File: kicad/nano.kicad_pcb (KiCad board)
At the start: 4 copper layers, 85 x 56 mm, 228 parts, among them J1 SD-104031, J2 PMIC_I2C, J3 USB_Micro, J4 USB_OTG, J5 JTAG, J6 TOUCH PANEL, J7 LiPo_THM, P1 EXPANSION, P2 DISPLAY, P3 J0011D01BNL, P4 USB-A-D-RA-30, P5 USB-A-D-RA-30, Q1 2SK3018, U1 IMX6UL_BGA289, U10 MIC2506, U11 MIC2506, U12 MIC2877, U2 DDR3_BGA96, U3 A7101CH, U4 W25M512JV, U5 W25M512JV, U6 PF1550, U7 LAN8720A, U8 USB2514B, U9 CP2102N-QFN20, Y1 32.768 kHz

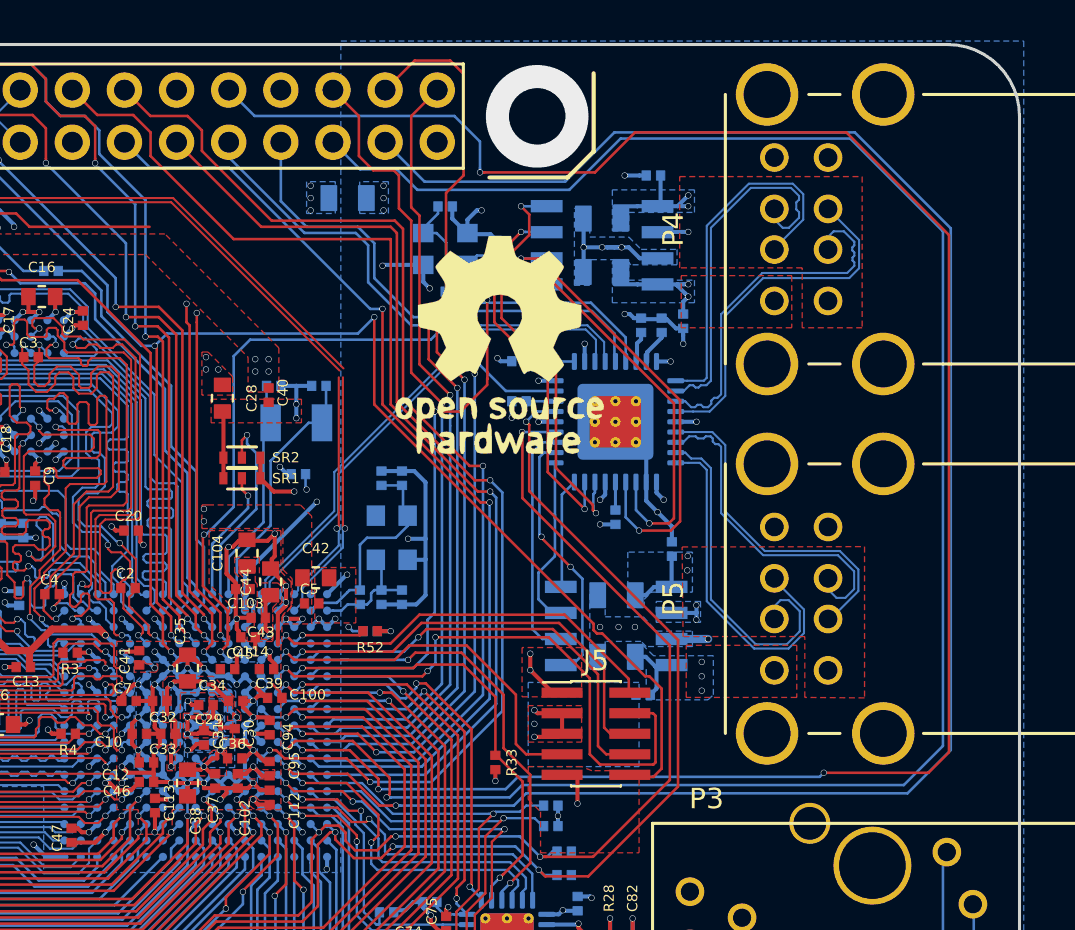
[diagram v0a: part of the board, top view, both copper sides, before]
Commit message: uart2/3 layout
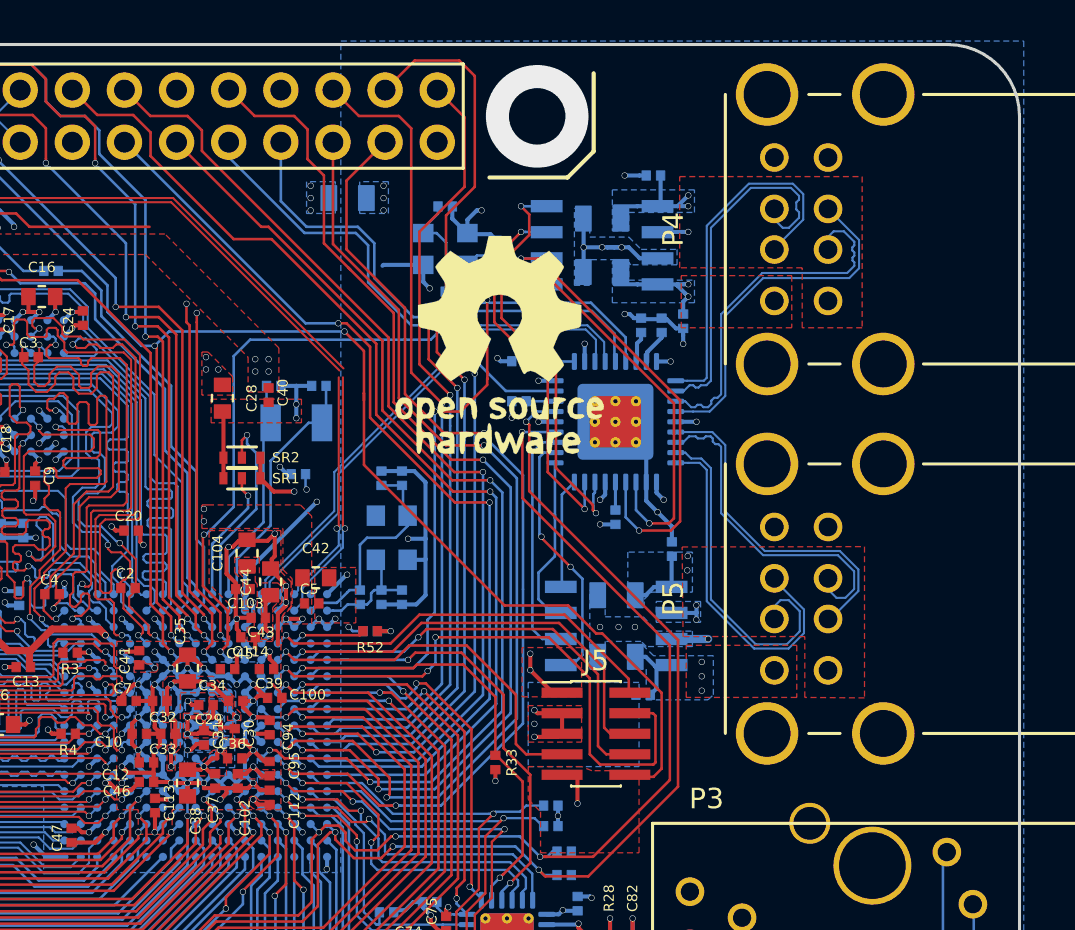
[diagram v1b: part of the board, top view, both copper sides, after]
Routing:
- net /IMX_Peripherals_1/UART3_CTS: track 99.6 -> 51.6 mm, vias 4 -> 3
- net UART2_RTS: track 94.4 -> 48.4 mm, vias 2 -> 3
- net /IMX_Peripherals_1/UART3_RTS: track 91.6 -> 48.4 mm, vias 2 -> 3
- net UART4_TXD: track 50.6 -> 47.5 mm
- net /IMX_Peripherals_1/UART5_RX: track 52.4 -> 49.6 mm
- net /IMX_Peripherals_1/UART5_TX: track 54.0 -> 51.3 mm
- net UART2_RXD: track 38.2 -> 39.0 mm
- net UART2_CTS: track 46.3 -> 47.0 mm
- net UART4_RXD: track 47.6 -> 46.9 mm
- net UART2_TXD: track 38.2 -> 38.7 mm
- net GND: vias 154 -> 153

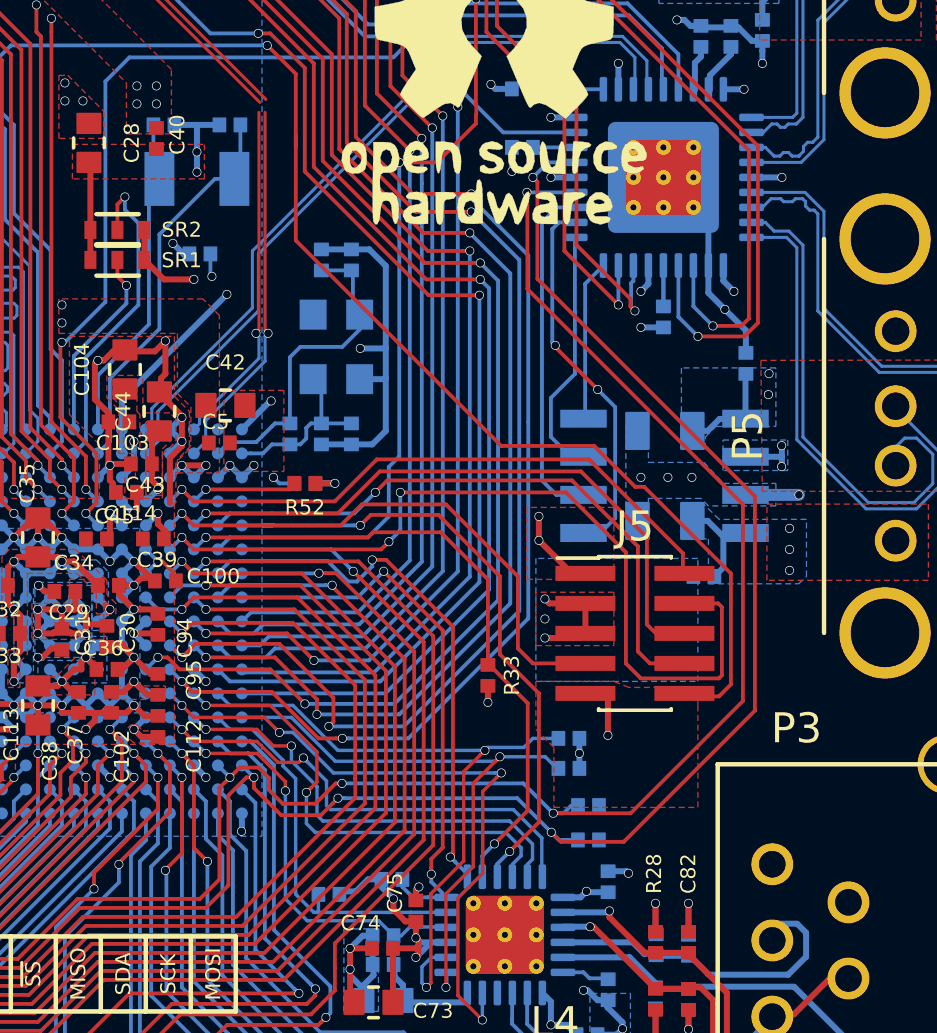
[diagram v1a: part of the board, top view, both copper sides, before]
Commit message: layout: move jtag connector
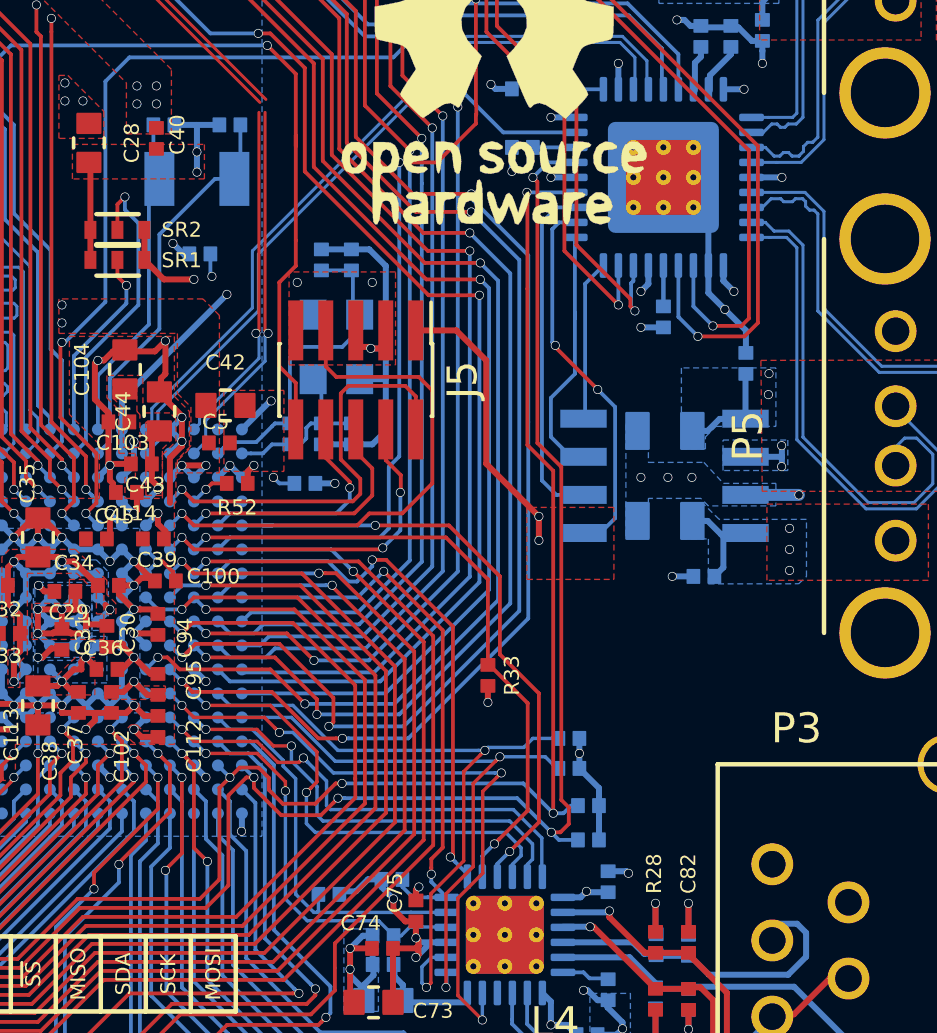
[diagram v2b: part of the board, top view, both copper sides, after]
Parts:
- moved J5 12.6 mm to (165.1, 97.6), turned to 270 degrees
- moved R52 2.25 mm to (161.1, 101.1)
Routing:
- net POR_B: track 92.4 -> 74.6 mm
- net /Clock_and_Control/JTAG_TCK: track 28.6 -> 11.9 mm
- net /Clock_and_Control/JTAG_TDI: track 20.7 -> 7.43 mm
- net /Clock_and_Control/JTAG_TDO: track 21.0 -> 8.79 mm
- net DCDC_3V3: track 49.8 -> 59.1 mm
- net BOARD_SDA: track 148.9 -> 142.0 mm
- net BOARD_SCL: track 151.1 -> 144.3 mm
- net /Clock_and_Control/JTAG_TMS: track 19.9 -> 14.2 mm
- net GND: track 236.9 -> 232.8 mm, vias 153 -> 152
- net /Clock_and_Control/JTAG_MOD: track 3.51 -> 1.34 mm

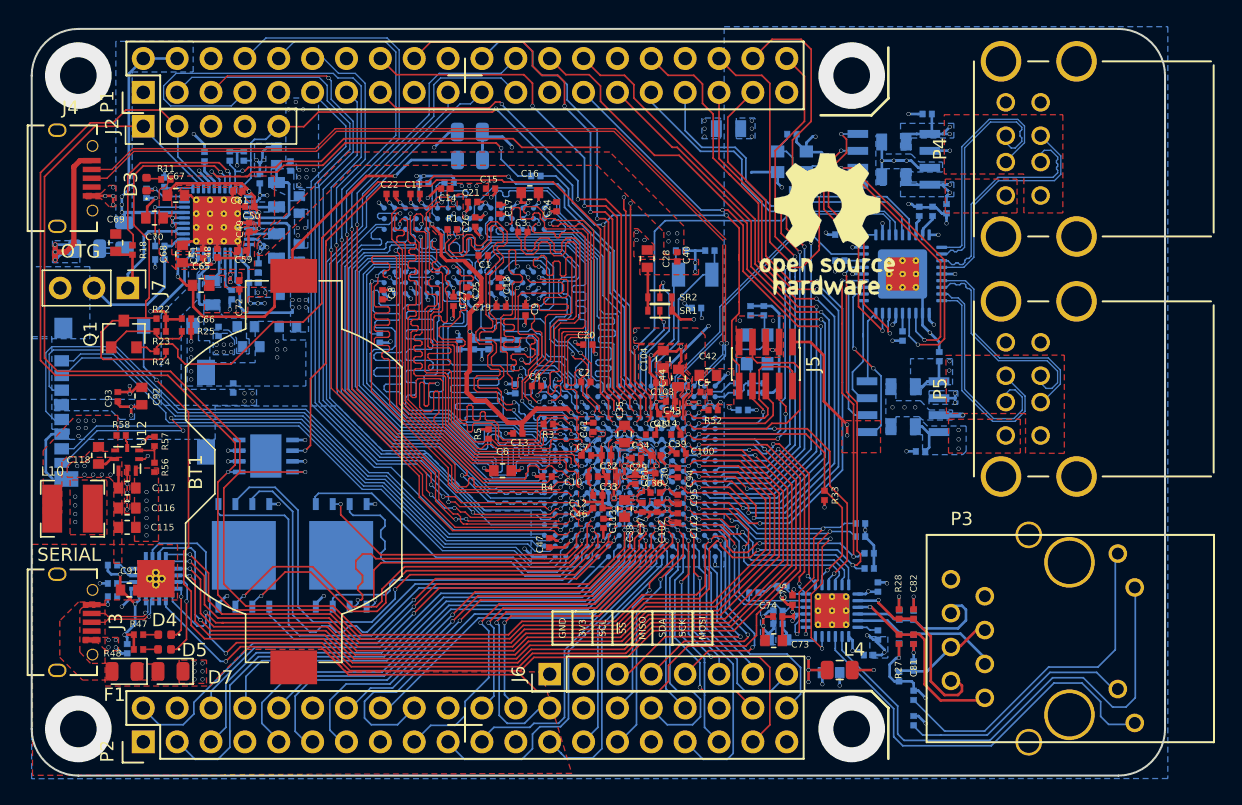
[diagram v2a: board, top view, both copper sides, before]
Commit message: layout: move usb hub, improve gpio connections
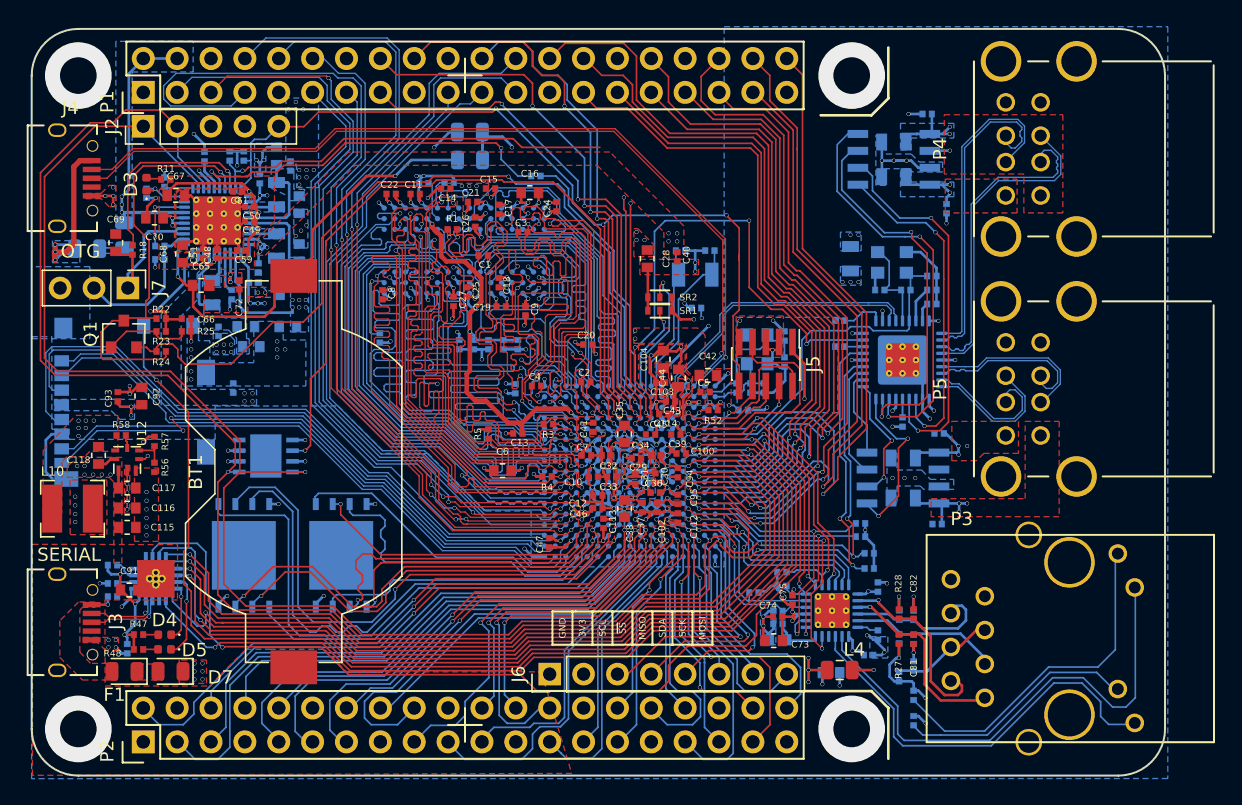
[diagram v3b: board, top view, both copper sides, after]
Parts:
- removed G***: LOGO, Custom Components:logo
- R33: moved to B.Cu
- moved C88 13.4 mm to (173.6, 92.1), turned to 180 degrees
- moved L9 13.4 mm to (171.4, 89.7), turned to 270 degrees
- moved C107 12.6 mm to (177.9, 109.6), turned to 180 degrees
- moved C89 11.8 mm to (177.5, 91.0), turned to 0 degrees
- moved R45 11.1 mm to (175.6, 92.1)
- moved XTAL1 10.6 mm to (174.5, 90.0)
- moved R44 6.95 mm to (177.5, 93.1), turned to 180 degrees
- moved R33 6.58 mm to (166.3, 113.2), turned to 180 degrees
- moved C86 6.45 mm to (175.3, 102.0)
- moved R43 6.45 mm to (170.6, 96.3)
- moved U8 6.45 mm to (175.3, 97.3)
- moved R40 6.45 mm to (170.6, 94.4)
- moved C87 5.98 mm to (177.5, 92.1), turned to 0 degrees
- moved L7 5.35 mm to (175.4, 107.7)
- moved L8 5.35 mm to (175.4, 104.7)
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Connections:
- L7 pad 2: /USB HUB/USB3_VBUS -> /USB HUB/USB2_VBUS
- L8 pad 2: /USB HUB/USB2_VBUS -> /USB HUB/USB3_VBUS
- U11 pad 1: /USB HUB/PORT4_PWR -> /USB HUB/PORT3_PWR
- U11 pad 2: /USB HUB/PORT4_OCS -> /USB HUB/PORT3_OCS
- U11 pad 3: /USB HUB/PORT3_OCS -> /USB HUB/PORT4_OCS
- U11 pad 4: /USB HUB/PORT3_PWR -> /USB HUB/PORT4_PWR
- U11 pad 5: /USB HUB/USB2_VBUS -> /USB HUB/USB3_VBUS
- U11 pad 8: /USB HUB/USB3_VBUS -> /USB HUB/USB2_VBUS
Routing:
- net UART2_RXD: track 39.0 -> 54.8 mm
- net GND: track 232.8 -> 217.7 mm, vias 152 -> 144
- net HUB_24MHZ: track 39.0 -> 27.2 mm, vias 2 -> 0
- net /USB HUB/PORT2_PWR: track 20.3 -> 30.8 mm
- net /USB HUB/PORT2_OCS: track 18.3 -> 28.7 mm
- net /USB HUB/XTALOUT: track 16.0 -> 7.05 mm
- net UART2_TXD: track 38.7 -> 47.3 mm
- net /IMX_Peripherals_1/UART3_TX: track 40.6 -> 48.9 mm, vias 2 -> 1
- net /USB HUB/PORT3_PWR: track 5.40 -> 12.5 mm, vias 0 -> 2
- net BOARD_SDA: track 142.0 -> 135.1 mm
- net USB0_D+: track 18.1 -> 24.6 mm
- net USB1_D-: track 17.7 -> 24.1 mm
- net USB1_D+: track 17.7 -> 24.2 mm
- net USB0_D-: track 18.0 -> 24.5 mm
- net USB3_D+: track 17.3 -> 10.9 mm
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- removed copper zone on B.Cu, net /USB HUB/USB2_VBUS
- removed copper zone on B.Cu, net /USB HUB/USB3_VBUS

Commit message: fix DRC
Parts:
- removed SR1, SR2: 4.7k, Custom Components:SR_0402
- added SB1: 4.7K, Custom Components:R_0402_narrow, B.Cu at (155.4, 90.5)
- added SB2: 4.7K, Custom Components:R_0402_narrow, B.Cu at (155.4, 91.5)
- added SB3: 4.7K, Custom Components:R_0402_narrow, B.Cu at (155.4, 89.5)
- added SB4: 4.7K, Custom Components:R_0402_narrow, B.Cu at (155.4, 88.5)
- R52: moved to B.Cu
- moved C114 2.95 mm to (160.3, 101.2), turned to 0 degrees
- moved C88 2.55 mm to (173.6, 89.5)
- moved C89 2.55 mm to (177.5, 88.5)
- moved R45 2.55 mm to (175.6, 89.5)
- moved XTAL1 2.55 mm to (174.5, 87.5)
- moved R52 2.36 mm to (163.3, 102.0)
- moved L9 2.11 mm to (173.1, 91.0), turned to 0 degrees
- moved Y1 1.25 mm to (158.5, 90.9)
- moved C40 1.25 mm to (157.2, 89.5)
- moved C96 1.25 mm to (157.4, 89.1)
- moved C97 1.25 mm to (159.6, 89.1)
- moved C28 1.00 mm to (156.2, 88.7)
- moved C86 0.75 mm to (176.1, 101.9), turned to 0 degrees
- moved C23 0.49 mm to (145.9, 99.1), turned to 180 degrees
- moved C47 0.36 mm to (148.6, 111.3), turned to 180 degrees
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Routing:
- net DCDC_3V3: track 54.9 -> 45.7 mm, vias 32 -> 33
- net HUB_RESET: track 39.6 -> 43.3 mm
- net UART2_TXD: track 47.3 -> 50.2 mm
- net /IMX_Peripherals_1/UART3_TX: track 48.9 -> 46.2 mm
- net /USB HUB/PORT1_OCS: track 28.7 -> 26.2 mm
- net /Clock_and_Control/BOOT1: track 6.50 -> 9.01 mm, vias 1 -> 0
- net /USB HUB/PORT1_PWR: track 25.7 -> 23.2 mm
- net /Clock_and_Control/JTAG_MOD: track 1.34 -> 3.73 mm, vias 1 -> 0
- net /USB HUB/XTALOUT: track 7.05 -> 9.40 mm
- net HUB_24MHZ: track 27.2 -> 29.2 mm
- net VDD_SNVS_IN: track 43.2 -> 45.0 mm
- net /Clock_and_Control/BOOT0: track 10.8 -> 12.3 mm, vias 1 -> 0
- net GND: track 217.7 -> 219.0 mm, vias 144 -> 145
- net /USB HUB/PORT2_OCS: track 28.7 -> 27.6 mm
- net /Clock_and_Control/VDDA_ADC: track 17.0 -> 18.0 mm
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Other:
- net class POWER: trace_width 0.2 -> 0.25
- rule trace_min: 0.1 -> 0.1016
- board text added: "MFG Rules Min track/spacing 4/4mil Min hole size 0.2mm 4 Layers Tenting vias"
